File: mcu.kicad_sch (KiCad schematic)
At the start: 5 parts, among them J3 USB_C_Receptacle_USB2.0_16P, M1 Module-stlink-0.1, M3 Module-mega-mcu144-0.6

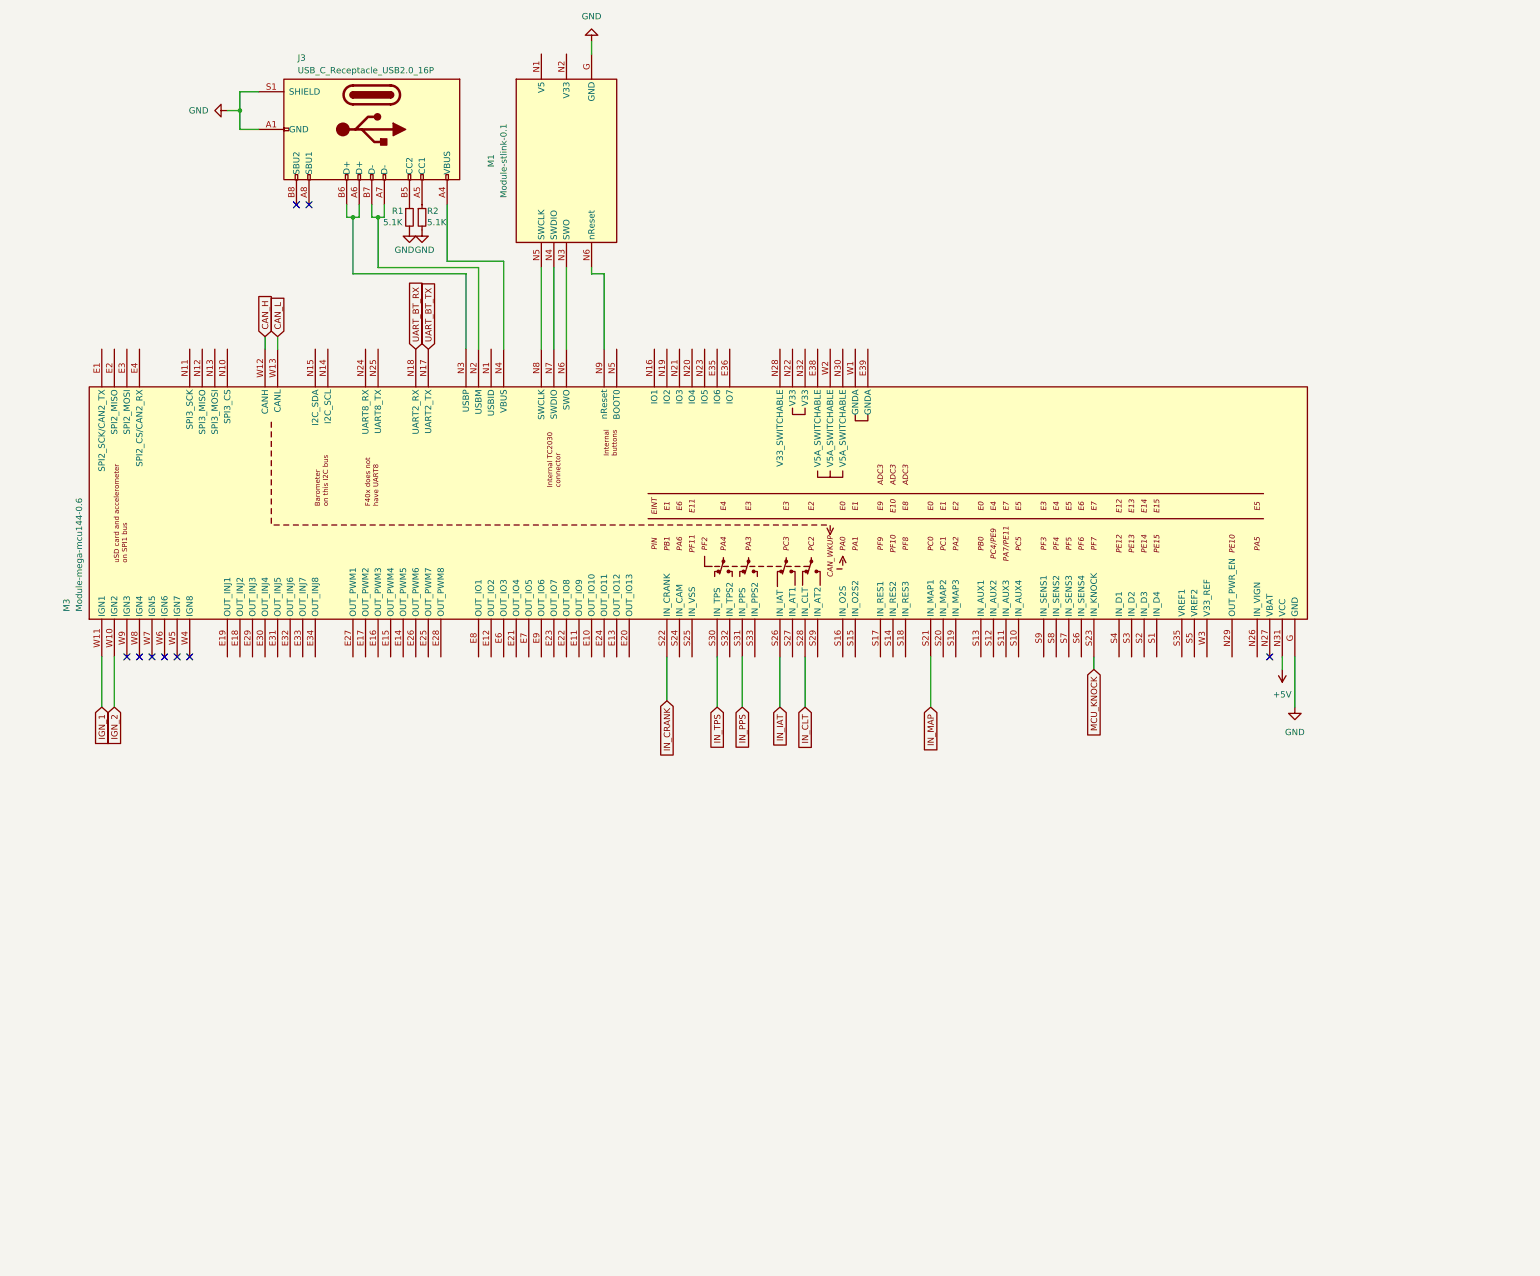
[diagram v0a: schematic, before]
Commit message: trying to fix aligment
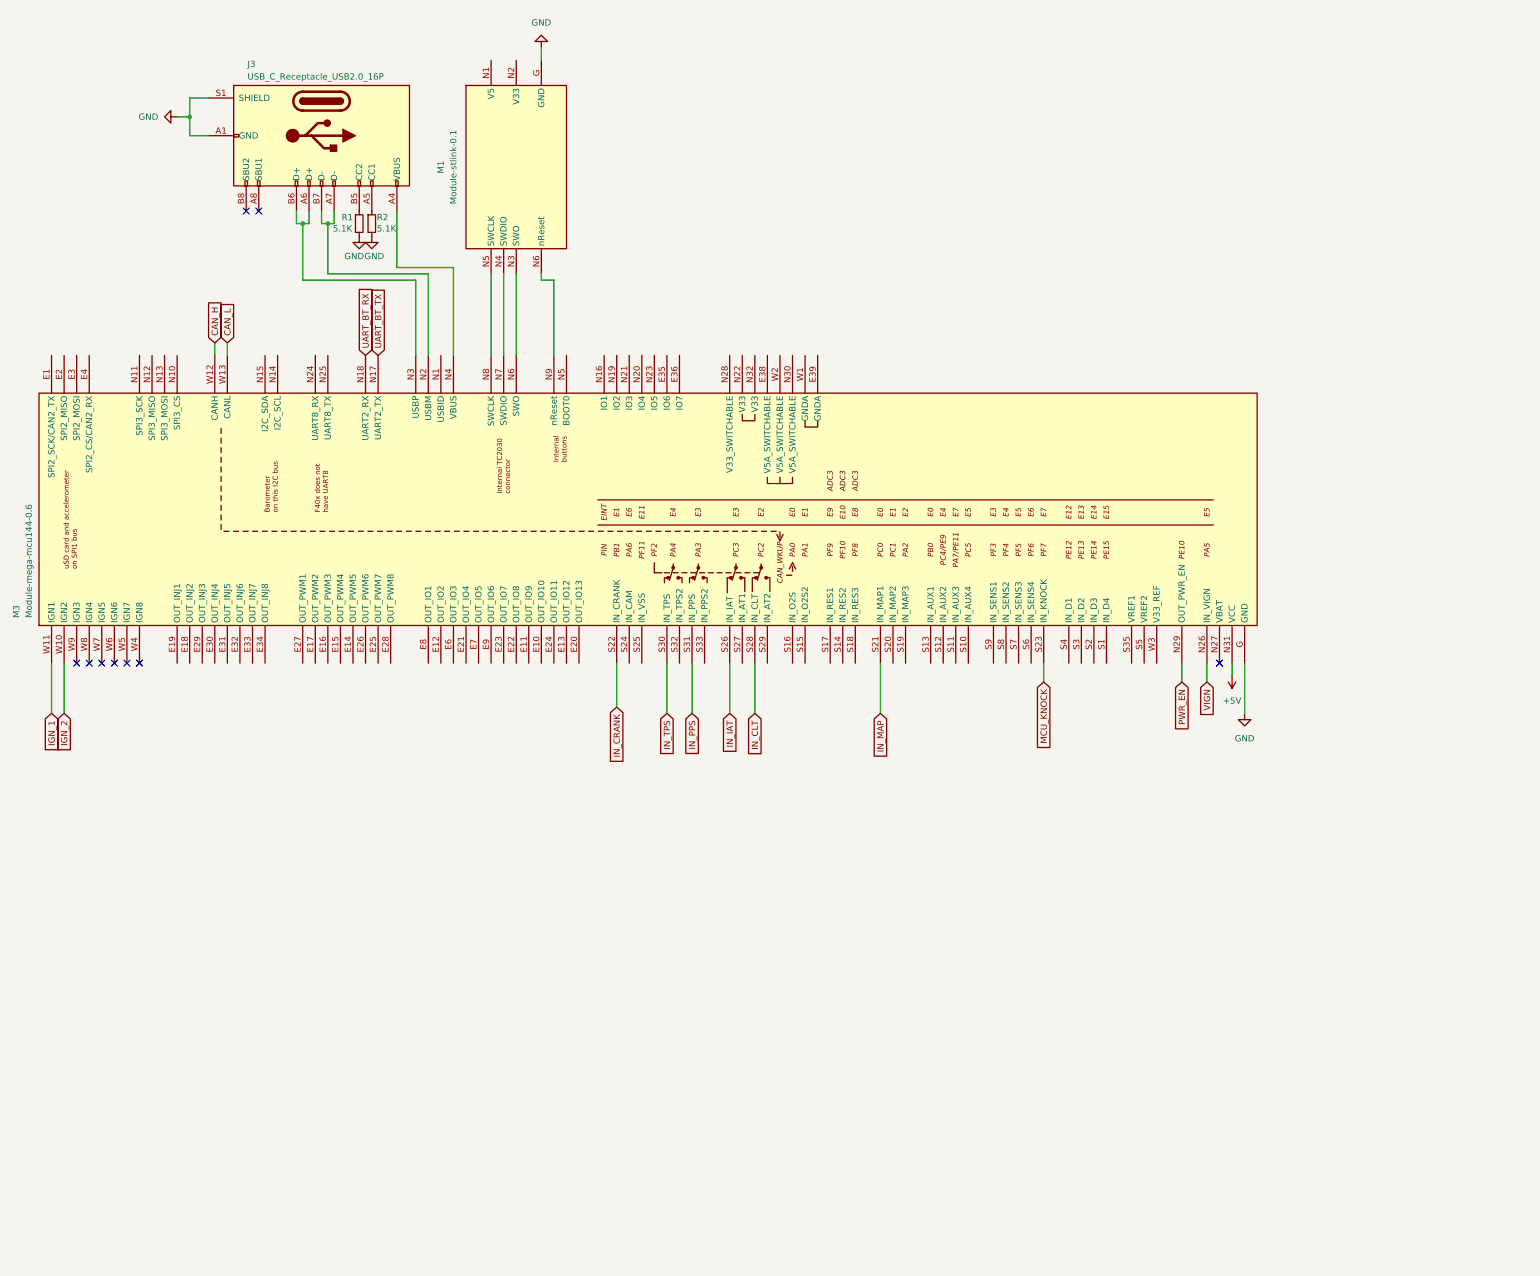
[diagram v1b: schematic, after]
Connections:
- net VIGN: now reaches M3.N26 (IN_VIGN)
- net PWR_EN: now reaches M3.N29 (OUT_PWR_EN)
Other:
- moved on the sheet: J3, M1, M3, R1, R2

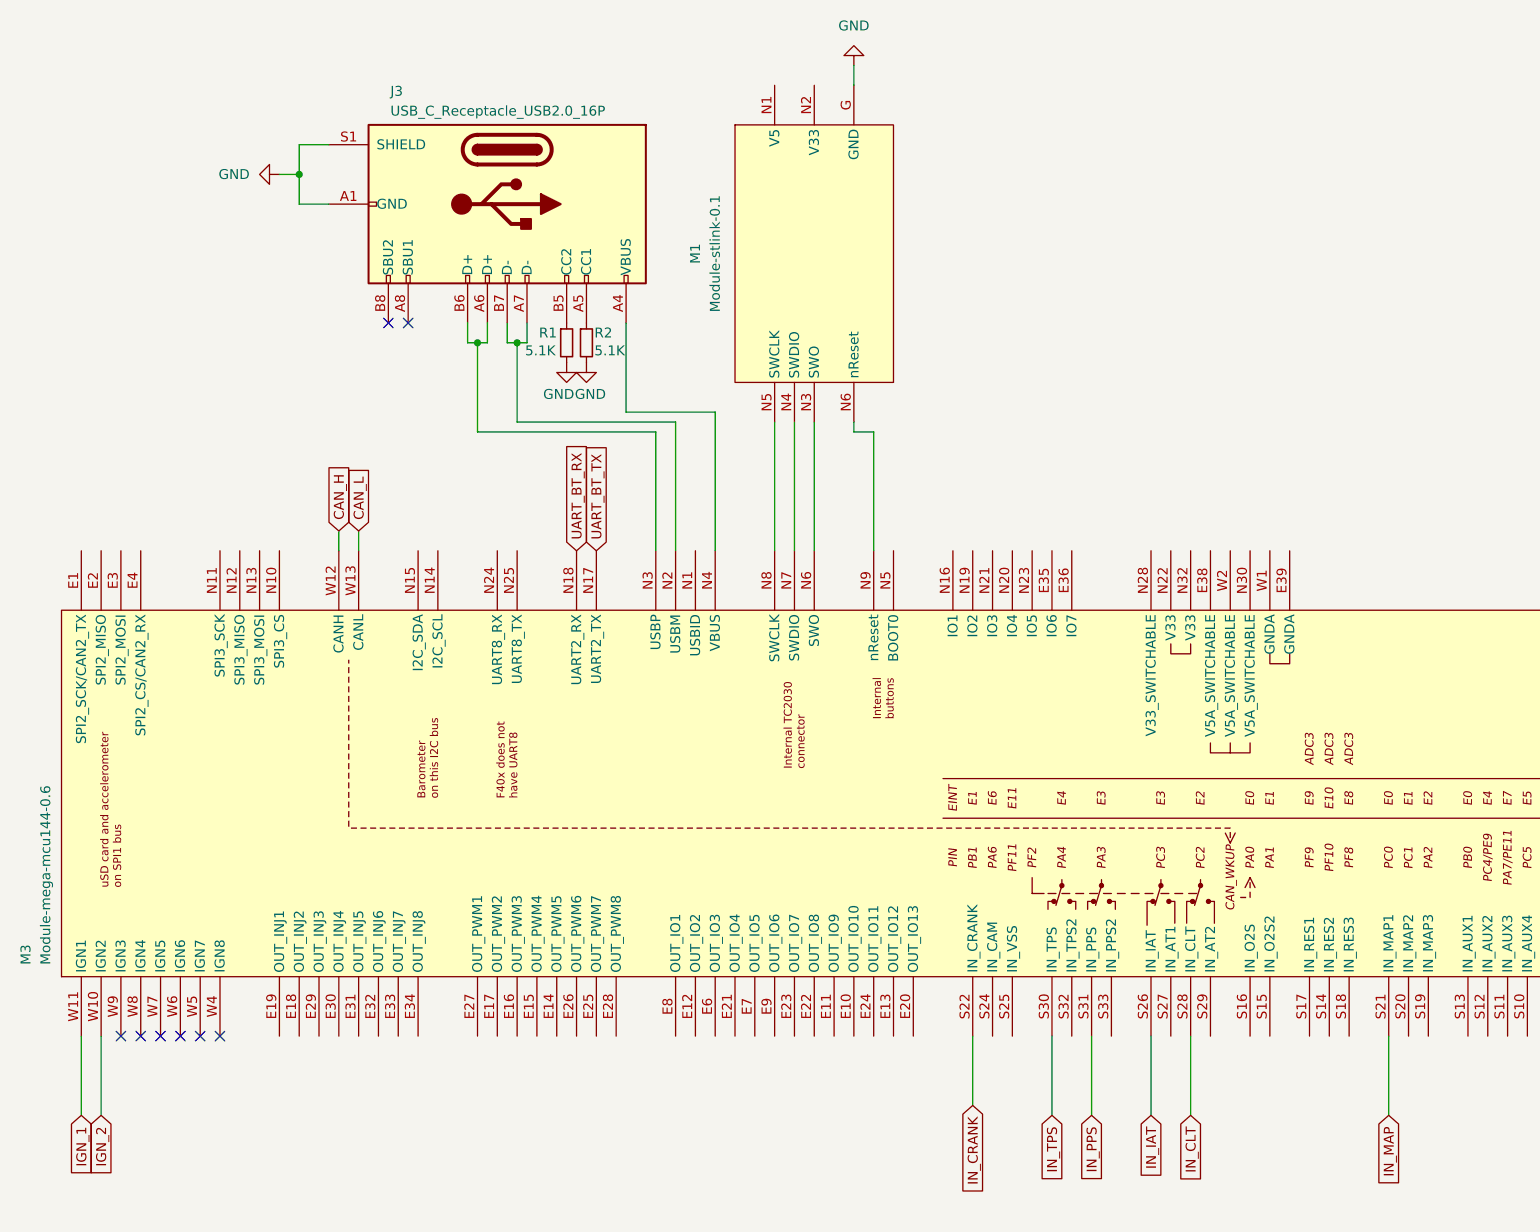
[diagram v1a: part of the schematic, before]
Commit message: Implementing some inputs and outputs
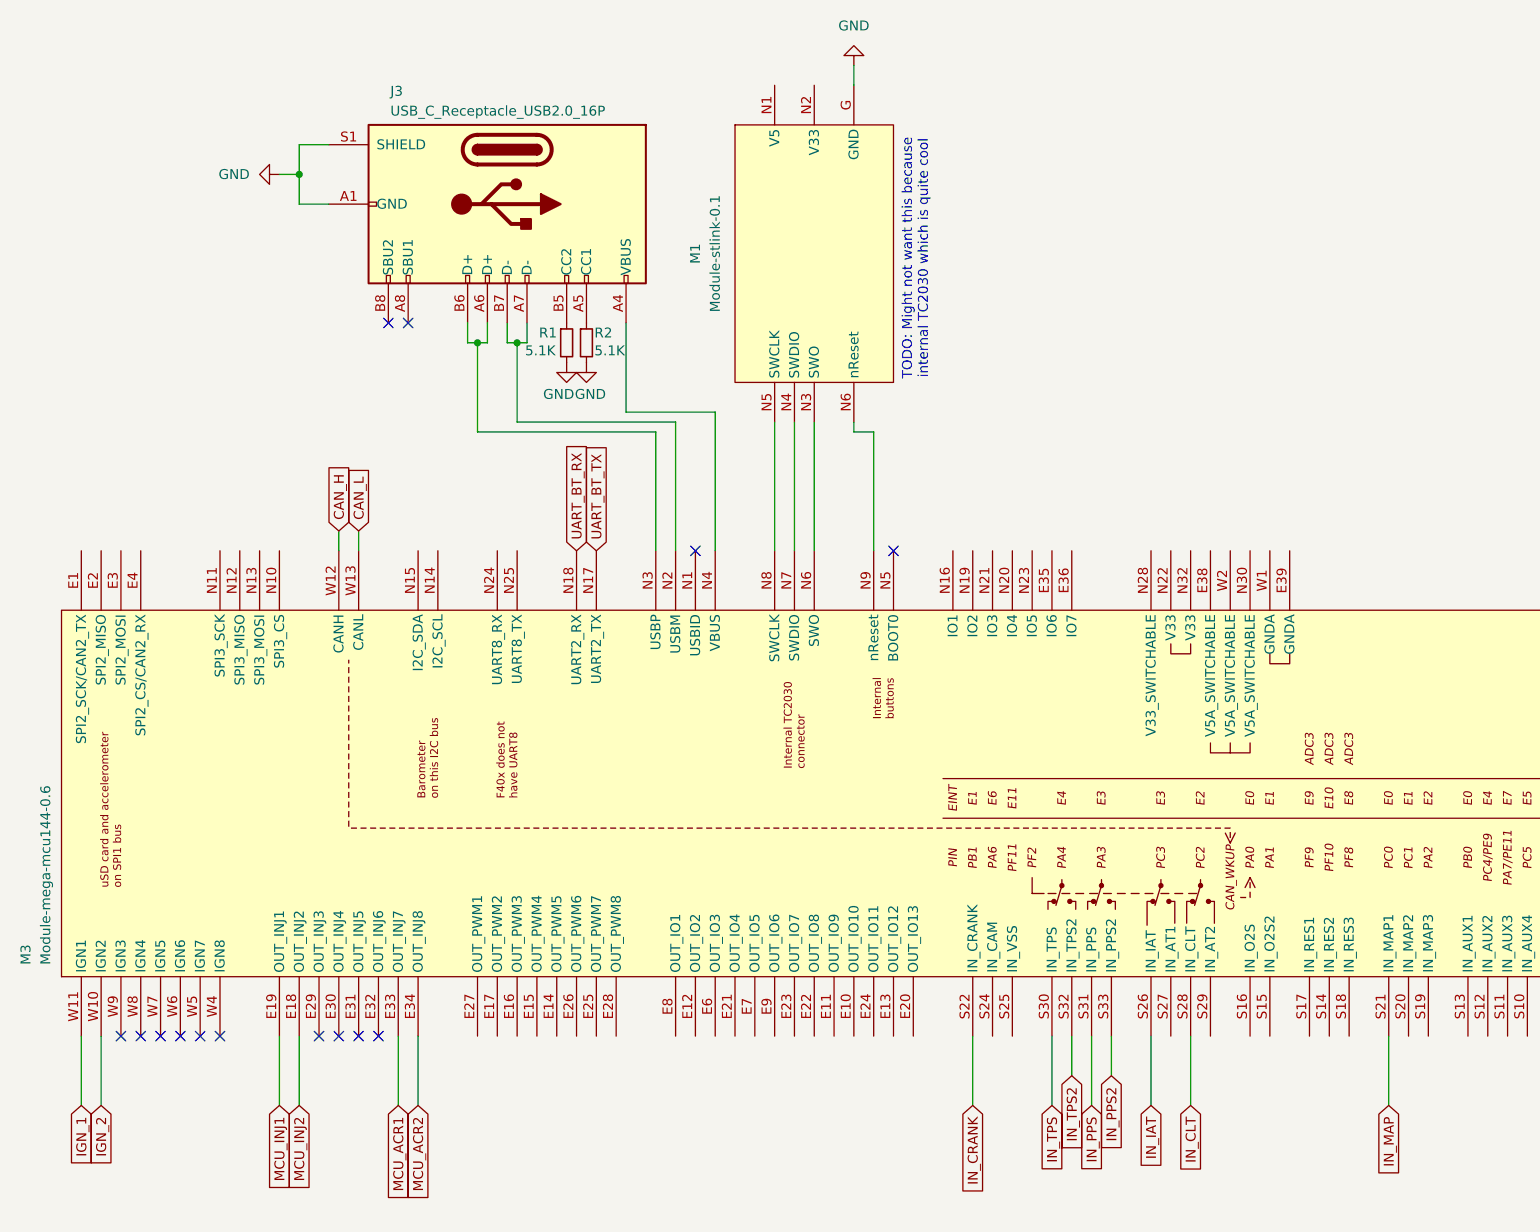
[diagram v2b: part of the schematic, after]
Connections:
- net MCU_INJ2: now reaches M3.E18 (OUT_INJ2)
- net MCU_INJ1: now reaches M3.E19 (OUT_INJ1)
- net MCU_ACR1: now reaches M3.E33 (OUT_INJ7)
- net MCU_ACR2: now reaches M3.E34 (OUT_INJ8)
- net IN_TPS2: now reaches M3.S32 (IN_TPS2)
- net IN_PPS2: now reaches M3.S33 (IN_PPS2)
- no-connect marks 9 -> 15
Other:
- note added: "TODO: Might not want this because internal TC2030 which is quite cool"

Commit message: still initial layout
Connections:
- net +3V3: now reaches M3.N22 (V33)
- net +3V3: now also M3.N32 (V33)
- net +3V3SW: now reaches M3.N28 (V33_SWITCHABLE)
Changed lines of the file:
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@@
+	)
+	(junction
+		(at 170.18 85.09)
+		(diameter 0)
+		(color 0 0 0 0)
 	)
 	(junction
@@
 	(wire
 		(pts
+			(xy 170.18 85.09) (xy 172.72 85.09)
+		)
+		(stroke
+			(width 0)
+			(type default)
+		)
+	)
+	(wire
+		(pts
 			(xy 87.63 58.42) (xy 86.36 58.42)
 		)
@@
 	(wire
 		(pts
+			(xy 170.18 82.55) (xy 170.18 85.09)
+		)
+		(stroke
+			(width 0)
+			(type default)
+		)
+	)
+	(wire
+		(pts
 			(xy 55.88 147.32) (xy 55.88 156.21)
 		)
@@
 		(pts
 			(xy 162.56 147.32) (xy 162.56 152.4)
+		)
+		(stroke
+			(width 0)
+			(type default)
+		)
+	)
+	(wire
+		(pts
+			(xy 167.64 78.74) (xy 167.64 85.09)
 		)
 		(stroke
@@
 				(justify right)
 				(hide yes)
+			)
+		)
+	)
+	(symbol
+		(lib_id "power:+3V3")
+		(at 167.64 78.74 0)
+		(unit 1)
+		(exclude_from_sim no)
+		(in_bom yes)
+		(on_board yes)
+		(dnp no)
+		(fields_autoplaced yes)
+		(property "Reference" "#PWR037"
+			(at 167.64 82.55 0)
+			(effects
+				(font
+					(size 1.27 1.27)
+				)
+				(hide yes)
+			)
+		)
+		(property "Value" "+3V3SW"
+			(at 167.64 73.66 0)
+			(effects
+				(font
+					(size 1.27 1.27)
+				)
+			)
+		)
+		(property "Footprint" ""
+			(at 167.64 78.74 0)
+			(effects
+				(font
+					(size 1.27 1.27)
+				)
+				(hide yes)
+			)
+		)
+		(property "Datasheet" ""
+			(at 167.64 78.74 0)
+			(effects
+				(font
+					(size 1.27 1.27)
+				)
+				(hide yes)
+			)
+		)
+		(property "Description" "Power symbol creates a global label with name \"+3V3\""
+			(at 167.64 78.74 0)
+			(effects
+				(font
+					(size 1.27 1.27)
+				)
+				(hide yes)
+			)
+		)
+		(pin "1"
+		)
+		(instances
+			(project "hellenbremen"
+				(path "/83409e39-90d0-4c85-be2e-bd292bea7c12/0ac5bb44-b3ea-4d91-97f2-4ef1e9f55a26"
+					(reference "#PWR037")
+					(unit 1)
+				)
 			)
 		)
@@
 					(unit 1)
 				)
+			)
+		)
+	)
+	(symbol
+		(lib_id "power:+3V3")
+		(at 170.18 82.55 0)
+		(unit 1)
+		(exclude_from_sim no)
+		(in_bom yes)
+		(on_board yes)
+		(dnp no)
+		(property "Reference" "#PWR036"
+			(at 170.18 86.36 0)
+			(effects
+				(font
+					(size 1.27 1.27)
+				)
+				(hide yes)
+			)
+		)
+		(property "Value" "+3V3"
+			(at 170.688 78.74 0)
+			(effects
+				(font
+					(size 1.27 1.27)
+				)
+			)
+		)
+		(property "Footprint" ""
+			(at 170.18 82.55 0)
+			(effects
+				(font
+					(size 1.27 1.27)
+				)
+				(hide yes)
+			)
+		)
+		(property "Datasheet" ""
+			(at 170.18 82.55 0)
+			(effects
+				(font
+					(size 1.27 1.27)
+				)
+				(hide yes)
+			)
+		)
+		(property "Description" "Power symbol creates a global label with name \"+3V3\""
+			(at 170.18 82.55 0)
+			(effects
+				(font
+					(size 1.27 1.27)
+				)
+				(hide yes)
+			)
+		)
+		(pin "1"
+		)
+		(instances
+			(project ""
+				(path "/83409e39-90d0-4c85-be2e-bd292bea7c12/0ac5bb44-b3ea-4d91-97f2-4ef1e9f55a26"
+					(reference "#PWR036")
+					(unit 1)
+				)
